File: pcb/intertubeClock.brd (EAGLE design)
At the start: 166.3 x 40.6 mm, 171 parts, among them Q1 BSA223SP, Q10 BSA223SP, Q11 BSA223SP, Q12 BSA223SP, Q13 BSA223SP, Q14 BSA223SP, Q15 BSA223SP, Q16 BSA223SP, Q17 BSS123, Q18 BSS123, Q19 BSS123, Q2 BSA223SP, Q20 BSS123, Q21 BSS123, Q3 BSA223SP, Q4 BSA223SP, Q5 BSA223SP, Q6 BSA223SP, Q7 BSA223SP, Q8 BSA223SP, Q9 BSA223SP, U1 HV5122PG, U2 HV5122PG

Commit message: -More layout work. -Added real parts library.
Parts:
- added JP11: Vba_off, pinhead:1X02
- added JP12: Vba, pinhead:1X02
- added JP13: Vs, pinhead:1X02
- D1, D2, D3, D4, D5, D6, D7, D8: value BAS40-06 -> MMBD3004A; device diode:SOT23 -> intertubeClock:SOT23
- JP2: value HV -> Vin; device pinhead:1X04 -> pinhead:1X02
- Q1, Q10, Q11, Q12, Q13, Q14, Q15, Q16, Q2, Q3, Q4, Q5, Q6, Q7, Q8, Q9: value BSA223SP -> TP5322K1-G; device transistor-fet:SC75_INFINEON -> intertubeClock:SOT23
- Q17, Q18, Q19, Q20, Q21: value BSS123 -> NX138AK; device transistor-small-signal:SOT23 -> intertubeClock:SOT23
- moved Q8 103.5 mm to (2.29, -58.2), turned to 0 degrees
- moved Q7 96.8 mm to (2.29, -50.8), turned to 0 degrees
- moved Q6 80.4 mm to (2.29, -43.4), turned to 0 degrees
- moved Q5 73.7 mm to (2.29, -36.1), turned to 0 degrees
- moved Q4 57.3 mm to (2.29, -28.7), turned to 0 degrees
- moved Q3 50.6 mm to (2.29, -21.3), turned to 0 degrees
- moved R17 17.5 mm to (28.7, 31.2), flipped to the top, turned to 0 degrees
- moved R15 17.3 mm to (22.1, 31.2), flipped to the top, turned to 0 degrees
- moved R54 16.0 mm to (24.1, 9.65)
- moved R55 16.0 mm to (29.2, 9.65)
- moved R56 16.0 mm to (26.7, 9.65)
- moved R57 16.0 mm to (34.3, 9.65)
- moved R58 16.0 mm to (31.8, 9.65)
- moved R59 16.0 mm to (41.9, 9.65)
- moved R60 16.0 mm to (47.0, 9.65)
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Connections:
- new net N$40: D3.3
- net GND: now also JP11.1, JP12.1, JP13.1; no longer JP2.4
- net HV_IN: no longer JP2.3
- net HV_VBA: now also JP12.2, Q1.2, Q10.2, Q11.2, Q12.2, Q13.2, Q14.2, Q15.2, Q16.2, Q2.2, Q3.2, Q4.2, Q5.2, Q6.2, Q7.2, Q8.2, Q9.2; no longer Q1.3, Q10.3, Q11.3, Q12.3, Q13.3, Q14.3, Q15.3, Q16.3, Q2.3, Q3.3, Q4.3, Q5.3, Q6.3, Q7.3, Q8.3, Q9.3
- net HV_VBA_OFF: now also JP11.2; no longer D3.3
- net HV_VS: now also JP13.2
- net N$17: now also Q1.3; no longer Q1.2
- net N$19: now also Q2.3; no longer Q2.2
- net N$21: now also Q3.3; no longer Q3.2
- net N$22: now also D2.2; no longer D2.1
- net N$24: now also Q4.3; no longer Q4.2
- net N$25: now also D2.1; no longer D2.2
- net N$26: now also D3.2; no longer D3.1
- net N$27: now also D3.1; no longer D3.2
- net N$28: now also D4.2; no longer D4.1
- net N$29: now also D4.1; no longer D4.2
- net N$30: now also Q9.3; no longer Q9.2
- net N$31: now also D5.2; no longer D5.1
- net N$32: now also D5.1; no longer D5.2
- net N$33: now also D6.2; no longer D6.1
- net N$34: now also D6.1; no longer D6.2
- net N$35: now also Q13.3; no longer Q13.2
- net N$36: now also D7.2; no longer D7.1
- net N$37: now also D7.1; no longer D7.2
- net N$38: now also D8.2; no longer D8.1
- net N$39: now also D8.1; no longer D8.2
- net N$41: now also Q5.3; no longer Q5.2
- net N$42: now also Q6.3; no longer Q6.2
- net N$43: now also Q7.3; no longer Q7.2
- net N$44: now also Q8.3; no longer Q8.2
- net N$45: now also Q10.3; no longer Q10.2
- net N$46: now also Q11.3; no longer Q11.2
- net N$47: now also Q12.3; no longer Q12.2
- net N$48: now also Q14.3; no longer Q14.2
- net N$49: now also Q15.3; no longer Q15.2
- net N$50: now also Q16.3; no longer Q16.2
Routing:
- net N$2: track 15.8 -> 0.00 mm, vias 2 -> 0
- net K01_DIG1: track 35.0 -> 44.8 mm, vias 0 -> 1
- net K45_DIG1: track 32.4 -> 42.1 mm, vias 0 -> 1
- net K89_DIG1: track 30.5 -> 38.5 mm, vias 0 -> 1
- net A2_SEL#_DIG1: track 27.3 -> 19.6 mm
- net A1_SEL#_DIG1: track 26.8 -> 19.6 mm
- net K23_DIG1: track 36.8 -> 42.3 mm, vias 0 -> 1
- net K67_DIG1: track 34.2 -> 38.6 mm, vias 0 -> 1
- net S_DIG1: track 7.61 -> 9.81 mm, vias 0 -> 1
- net N$1: track 2.02 -> 0.00 mm, vias 2 -> 0
- net HV_VBA: track 1.41 -> 0.00 mm
- net A2_DIG1: track 5.32 -> 4.34 mm
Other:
- board size 166.3 x 40.6 mm -> 166.3 x 53.8 mm

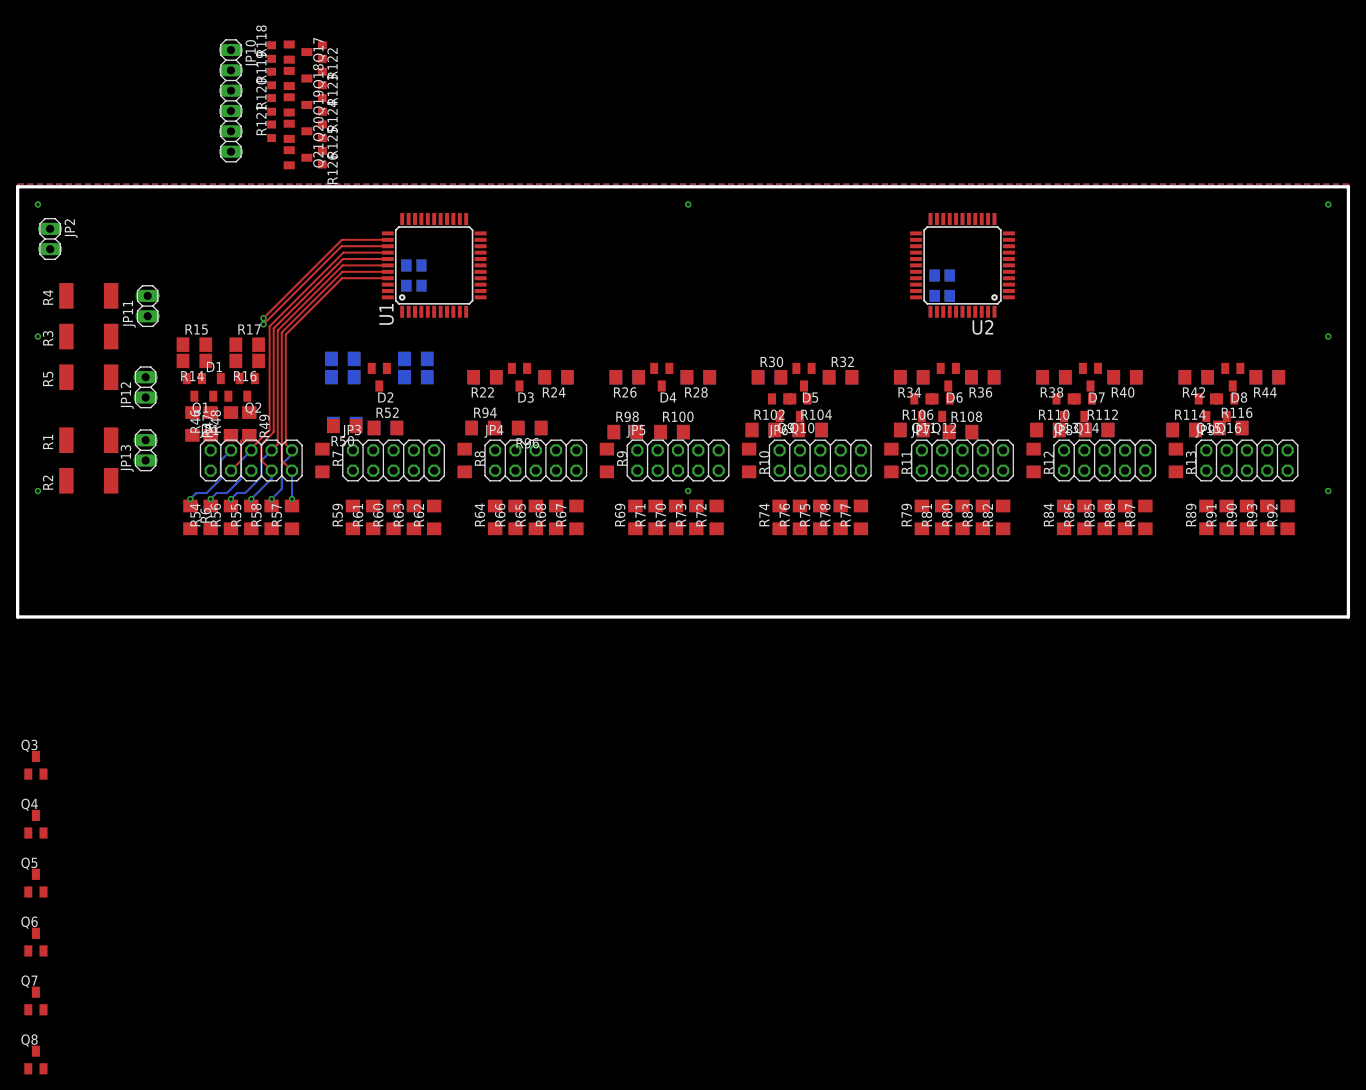
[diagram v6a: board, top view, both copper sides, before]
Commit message: -Continued layout. -Pinswapped diodes.
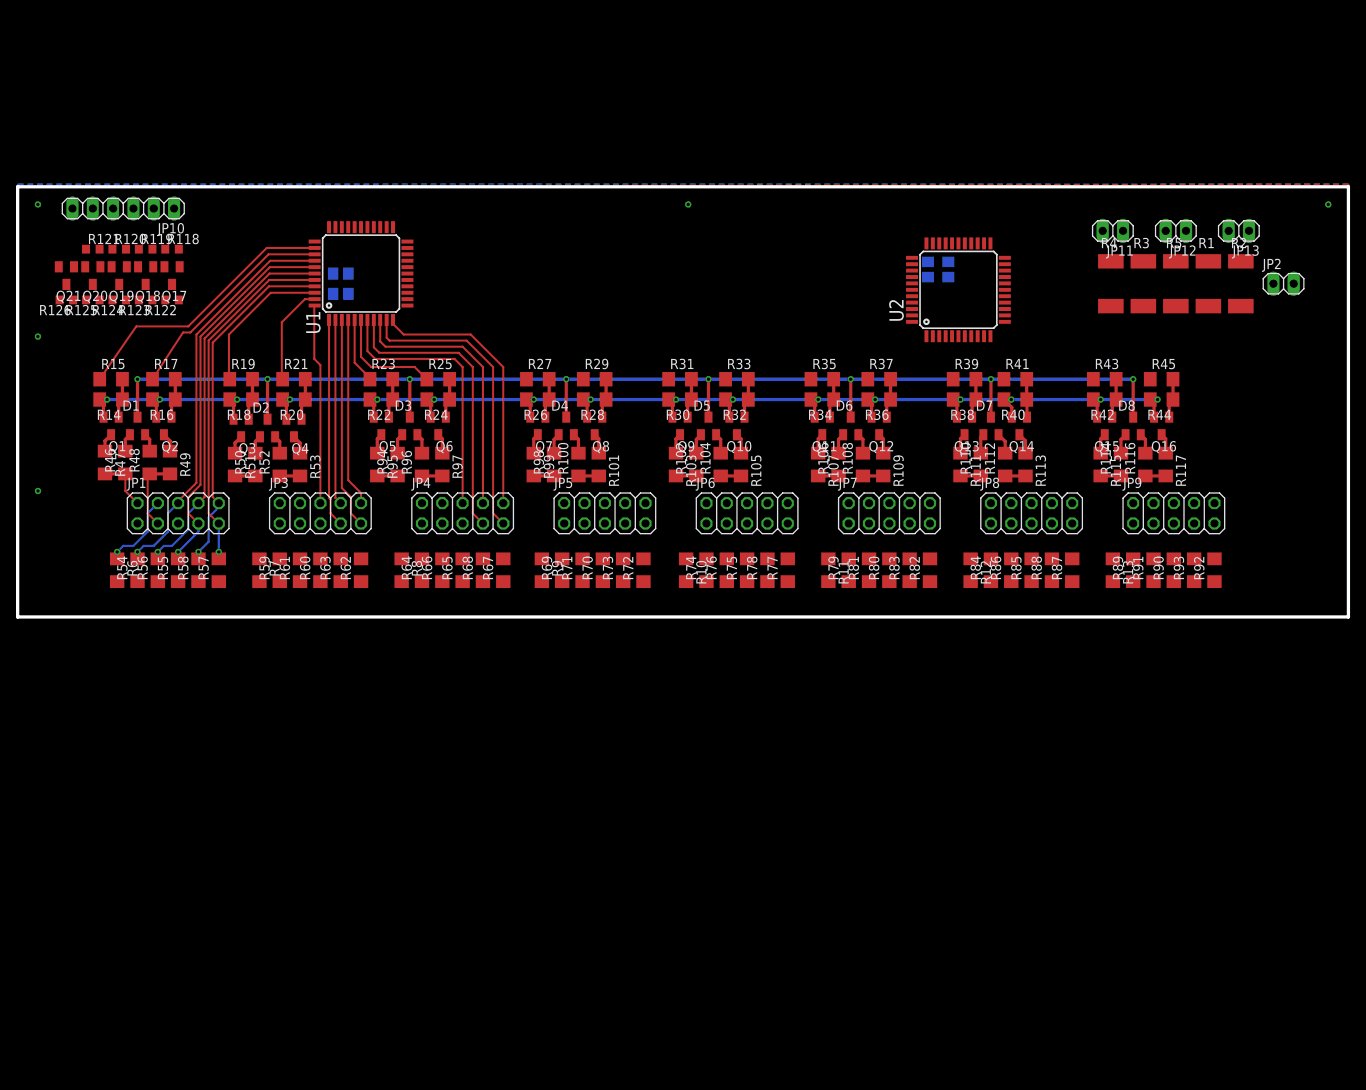
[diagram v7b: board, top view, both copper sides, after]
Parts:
- moved JP2 154.3 mm to (158.2, 38.9), turned to 0 degrees
- moved R2 146.1 mm to (152.9, 38.9), turned to 270 degrees
- moved R1 141.3 mm to (148.8, 38.9), turned to 270 degrees
- moved JP13 139.4 mm to (152.7, 45.5), turned to 180 degrees
- moved R5 136.4 mm to (144.8, 38.9), turned to 270 degrees
- moved R3 132.0 mm to (140.7, 38.9), turned to 270 degrees
- moved JP12 130.3 mm to (144.8, 45.5), turned to 180 degrees
- moved R4 127.8 mm to (136.7, 38.9), turned to 270 degrees
- moved JP11 121.0 mm to (136.9, 45.5), turned to 180 degrees
- moved Q8 105.6 mm to (72.1, 21.1), turned to 180 degrees
- moved Q7 95.4 mm to (65.0, 21.1), turned to 180 degrees
- moved Q6 81.8 mm to (52.6, 21.1), turned to 180 degrees
- moved Q5 71.6 mm to (45.5, 21.1), turned to 180 degrees
- moved Q4 59.1 mm to (34.5, 20.8), turned to 180 degrees
- moved Q3 49.4 mm to (27.9, 20.8), turned to 180 degrees
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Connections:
- removed net N$40: D3.3
- net HV_VBA_OFF: now also D3.3
- net N$22: now also D2.1; no longer D2.2
- net N$25: now also D2.2; no longer D2.1
- net N$26: now also D3.1; no longer D3.2
- net N$27: now also D3.2; no longer D3.1
- net N$28: now also D4.1; no longer D4.2
- net N$29: now also D4.2; no longer D4.1
- net N$31: now also D5.1; no longer D5.2
- net N$32: now also D5.2; no longer D5.1
- net N$33: now also D6.1; no longer D6.2
- net N$34: now also D6.2; no longer D6.1
- net N$36: now also D7.1; no longer D7.2
- net N$37: now also D7.2; no longer D7.1
- net N$38: now also D8.1; no longer D8.2
- net N$39: now also D8.2; no longer D8.1
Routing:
- net HV_VBA: track 0.00 -> 185.0 mm, vias 0 -> 16
- net HV_VBA_OFF: track 0.00 -> 162.7 mm, vias 0 -> 8
- net K67_DIG3: track 0.00 -> 37.1 mm
- net K23_DIG3: track 0.00 -> 36.9 mm
- net K45_DIG3: track 0.00 -> 33.9 mm
- net K01_DIG3: track 0.00 -> 33.6 mm
- net K89_DIG3: track 0.00 -> 33.5 mm
- net K67_DIG2: track 0.00 -> 26.4 mm
- net K23_DIG2: track 0.00 -> 26.0 mm
- net K01_DIG2: track 0.00 -> 25.0 mm
- net K89_DIG2: track 0.00 -> 23.6 mm
- net K45_DIG2: track 0.00 -> 23.2 mm
- net A1_SEL#_DIG2: track 0.00 -> 18.5 mm
- net A1_SEL#_DIG1: track 19.6 -> 34.4 mm, vias 1 -> 0
- net A2_SEL#_DIG3: track 0.00 -> 14.0 mm
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
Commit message: -Continued layout.
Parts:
- moved Q16 1.78 mm to (141.2, 21.1)
- moved R44 1.78 mm to (141.2, 24.4)
- moved R45 1.78 mm to (141.2, 26.9)
- moved D5 1.78 mm to (84.6, 21.1)
- moved D6 1.78 mm to (102.4, 21.1)
- moved Q11 1.78 mm to (98.8, 21.1)
- moved Q13 1.78 mm to (116.6, 21.1)
- moved Q9 1.78 mm to (81.0, 21.1)
- moved R100 1.78 mm to (68.3, 16.3)
- moved R101 1.78 mm to (70.9, 16.3)
- moved R103 1.78 mm to (80.5, 16.3)
- moved R104 1.78 mm to (86.1, 16.3)
- moved R105 1.78 mm to (88.6, 16.3)
- moved R106 1.78 mm to (100.8, 16.3)
- moved R108 1.78 mm to (103.9, 16.3)
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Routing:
- net K23_DIG5: track 0.00 -> 72.7 mm
- net K01_DIG5: track 0.00 -> 68.2 mm
- net K67_DIG4: track 0.00 -> 53.6 mm
- net K89_DIG4: track 0.00 -> 51.9 mm
- net K23_DIG4: track 0.00 -> 50.7 mm
- net K45_DIG4: track 0.00 -> 49.1 mm
- net K67_DIG5: track 0.00 -> 48.7 mm
- net K45_DIG5: track 0.00 -> 46.7 mm
- net K01_DIG4: track 0.00 -> 46.1 mm
- net K89_DIG5: track 0.00 -> 44.6 mm
- net K67_DIG7: track 0.00 -> 37.1 mm, vias 0 -> 2
- net K89_DIG7: track 0.00 -> 36.5 mm, vias 0 -> 2
- net K23_DIG7: track 0.00 -> 33.5 mm
- net K23_DIG6: track 0.00 -> 30.9 mm
- net A2_SEL#_DIG8: track 0.00 -> 30.7 mm, vias 0 -> 3
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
